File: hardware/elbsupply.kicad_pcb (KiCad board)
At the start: 2 copper layers, 105 x 64.4 mm, 80 parts, among them CON1 AVR-ISP-6, IC1 ATMEGA8-AI, P1 OUT_POS, P2 OUT_GND, P3 POWER_IN, Q1 KST2907A, SW1 SW_L, SW2 SW_R, U1 LM393, U2 TPS54331DDA, U3 LT1490, U4 LM358, U5 TS78L05CS, U6 LT3083

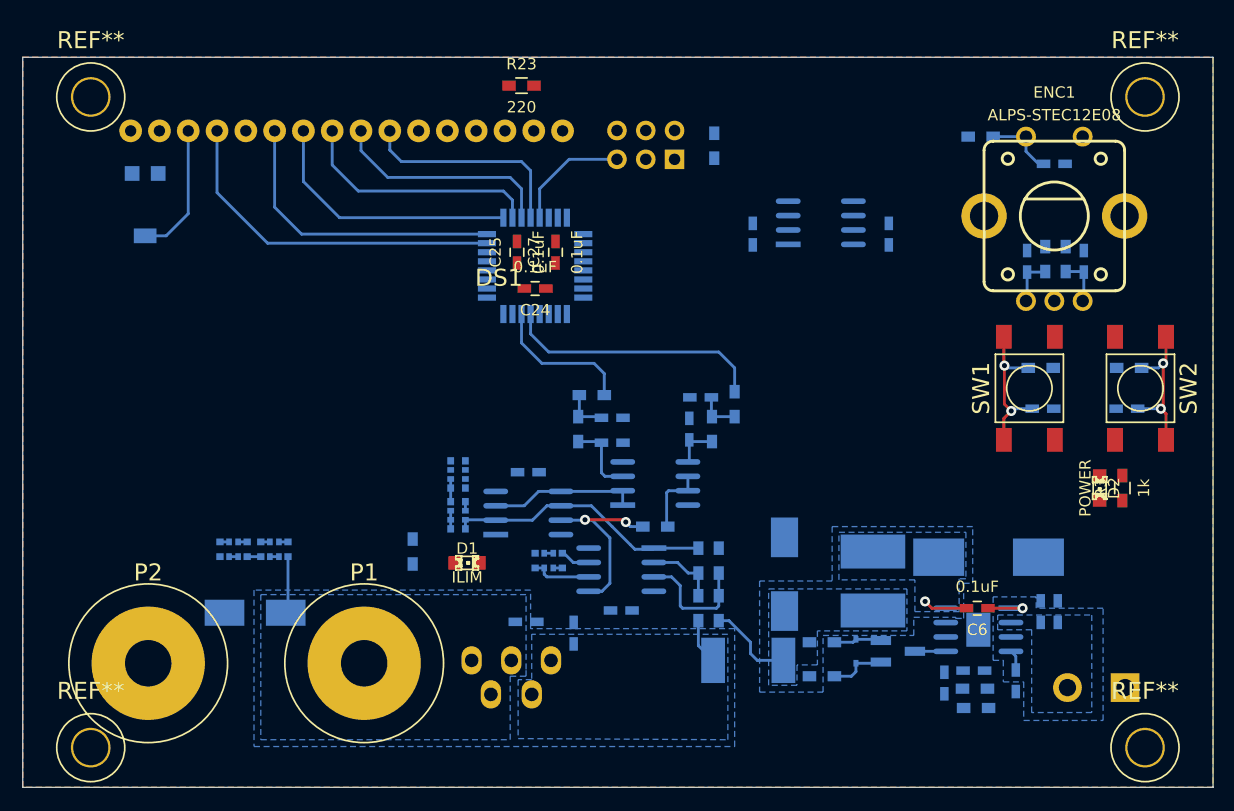
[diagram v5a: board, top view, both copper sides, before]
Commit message: LT3083 output capacitors exchanged for electrolytics
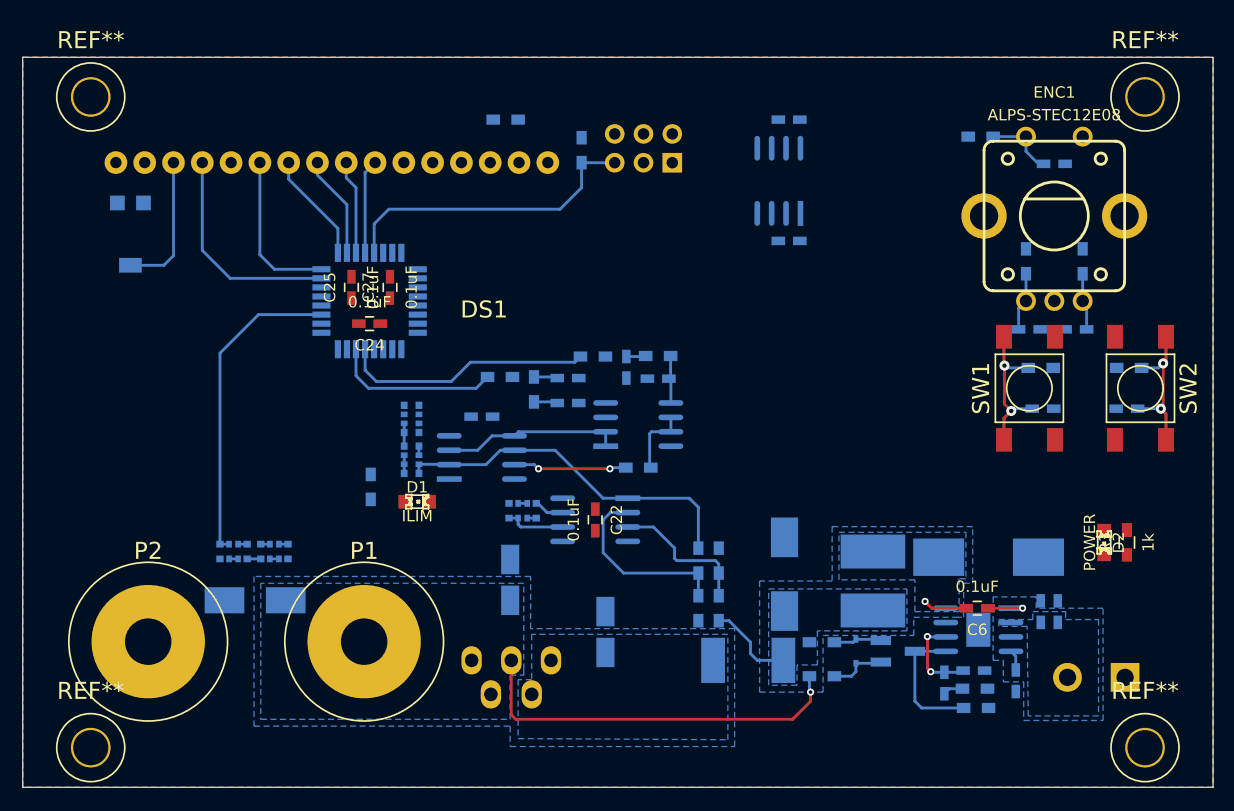
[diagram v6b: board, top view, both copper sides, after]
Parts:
- C20, C26: footprint Capacitors_SMD:C_0603_HandSoldering -> Capacitors_SMD:c_elec_4x4.5
- C22: moved to F.Cu
- R23: moved to B.Cu
- moved C24 14.9 mm to (71.6, 54.5)
- moved IC1 14.9 mm to (71.6, 52.5)
- moved C25 14.9 mm to (70.0, 51.3)
- moved C27 14.9 mm to (73.4, 51.3)
- moved C18 13.4 mm to (108.6, 36.5), turned to 180 degrees
- moved R21 13.2 mm to (91.3, 57.4), turned to 180 degrees
- moved R22 11.7 mm to (90.3, 39.2)
- moved C22 8.32 mm to (91.5, 71.8), turned to 270 degrees
- moved R7 8.26 mm to (83.1, 59.2), turned to 180 degrees
- moved R20 8.01 mm to (97.0, 57.4), turned to 180 degrees
- moved C23 7.07 mm to (94.2, 58.4), turned to 270 degrees
- moved D1 6.97 mm to (75.8, 70.2)
- moved R2 6.80 mm to (71.7, 68.9)
- moved RP3 6.39 mm to (75.3, 66.5)
- moved RP1 6.39 mm to (75.3, 62.9)
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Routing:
- net /LIN_OUT: track 5.03 -> 34.3 mm, vias 0 -> 1
- net /V_ADC: track 0.80 -> 28.0 mm
- net /~RST~: track 10.4 -> 27.3 mm
- net /LCD_D0: track 23.4 -> 9.76 mm
- net /LCD_D1: track 21.7 -> 9.04 mm
- net /LCD_E: track 26.4 -> 14.1 mm
- net /LCD_RS: track 31.1 -> 19.3 mm
- net /LCD_D2: track 19.9 -> 8.32 mm
- net /LCD_D3: track 19.0 -> 8.32 mm
- net Net-(R17-Pad2): track 6.31 -> 16.5 mm
- net Net-(Q1-Pad3): track 2.73 -> 11.7 mm
- net /I_Meas: track 23.5 -> 31.7 mm
- net Net-(C4-Pad2): track 0.00 -> 7.80 mm, vias 0 -> 2
- net /V_control: track 16.6 -> 10.0 mm
- net Net-(C14-Pad1): track 6.75 -> 2.09 mm
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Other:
- net class Default: via_dia 0.889 -> 0.635; via_drill 0.635 -> 0.381
- rule via_min_drill: 0.508 -> 0.3302
- rule via_min_size: 0.889 -> 0.508

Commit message: rev. A routing finished
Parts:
- D2: value POWER -> (none)
- ENC1: value ALPS-STEC12E08 -> (none)
- R2, R22: moved to F.Cu
- R3: moved to B.Cu
- moved D2 33.8 mm to (141.5, 40.4), turned to 90 degrees
- moved R3 29.5 mm to (134.5, 44.6)
- moved R22 18.3 mm to (73.1, 45.5), turned to 0 degrees
- moved R2 15.8 mm to (61.6, 56.8)
- moved D1 15.6 mm to (61.4, 76.2)
- moved R4 7.94 mm to (126.7, 51.6), turned to 270 degrees
- moved R6 7.72 mm to (129.5, 44.6), turned to 90 degrees
- moved R5 7.12 mm to (137.3, 51.4), turned to 270 degrees
- moved C9 6.88 mm to (133.9, 56.8)
- moved C7 5.34 mm to (129.8, 56.8)
- moved C24 3.21 mm to (71.8, 51.3), turned to 270 degrees
- moved R23 2.20 mm to (85.8, 36.4), turned to 180 degrees
- moved C6 0.40 mm to (125.2, 79.2)
- moved C25 0.20 mm to (70.2, 51.3)
- moved C17 0.10 mm to (81.5, 62.6)
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- renumbered REF** to M3
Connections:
- IC1 pad 1: /ENC_A -> /ENC_B
- IC1 pad 2: /ENC_B -> /ENC_A
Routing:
- net +24V: track 0.00 -> 199.3 mm, vias 0 -> 4
- net +5V: track 0.00 -> 142.1 mm, vias 0 -> 2
- net /SW_R: track 13.6 -> 75.7 mm
- net /ENC_SW: track 6.21 -> 67.0 mm, vias 0 -> 1
- net /ENC_B: track 5.26 -> 66.0 mm, vias 0 -> 1
- net /ENC_A: track 5.31 -> 60.4 mm, vias 0 -> 1
- net /SW_L: track 13.8 -> 63.1 mm
- net GND: track 0.00 -> 44.8 mm, vias 0 -> 26
- net /MOSI: track 0.00 -> 44.2 mm, vias 0 -> 1
- net /MISO: track 0.00 -> 41.7 mm, vias 0 -> 1
- net /SCK: track 0.00 -> 40.3 mm, vias 0 -> 1
- net Net-(D1-Pad2): track 0.00 -> 22.0 mm, vias 0 -> 1
- net /I_ADC: track 1.60 -> 22.8 mm, vias 0 -> 2
- net Net-(RP2-Pad8): track 2.66 -> 22.9 mm, vias 0 -> 1
- net Net-(D1-Pad1): track 0.00 -> 18.8 mm
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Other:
- net class Power_24V added: clearance 0.254, trace_width 0.635, via_dia 0.635, via_drill 0.381
- net class Power_5V added: clearance 0.254, trace_width 0.508, via_dia 0.635, via_drill 0.381

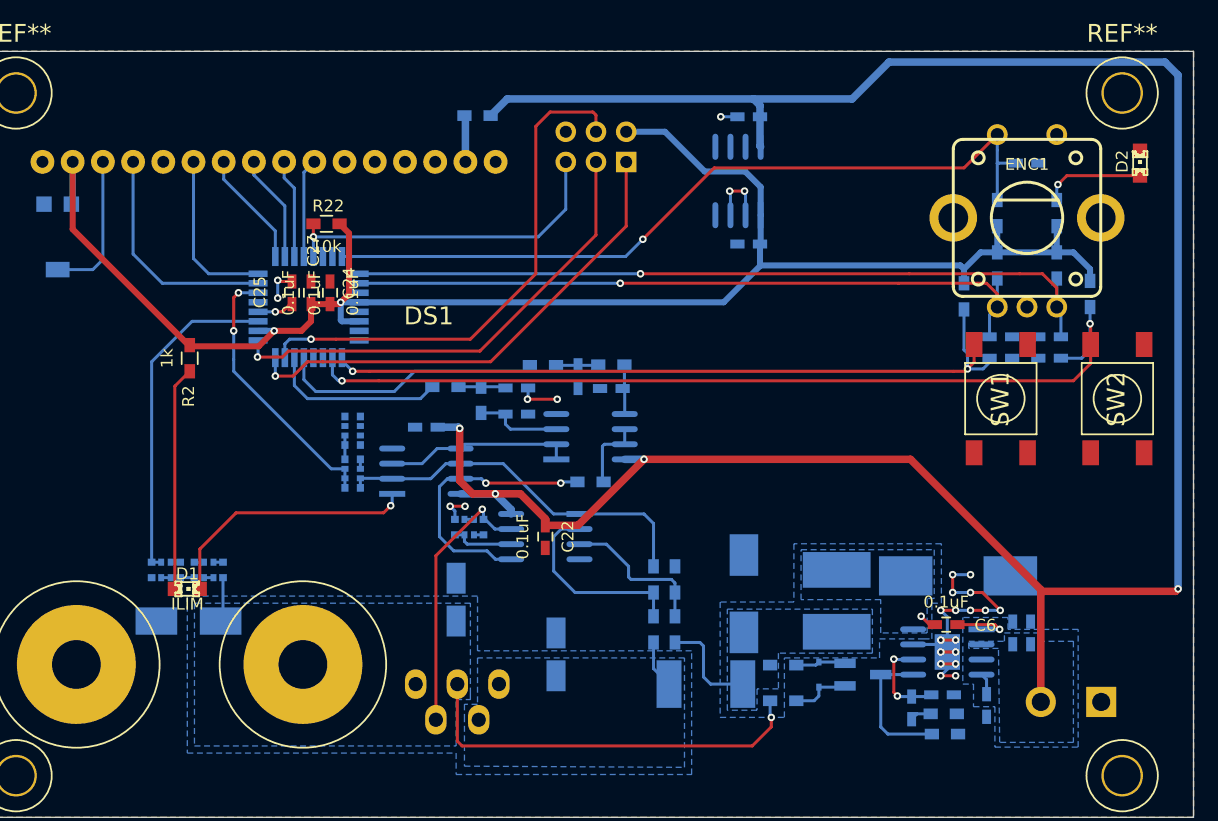
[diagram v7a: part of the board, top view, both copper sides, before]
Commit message: added two more switches for cleaner UI
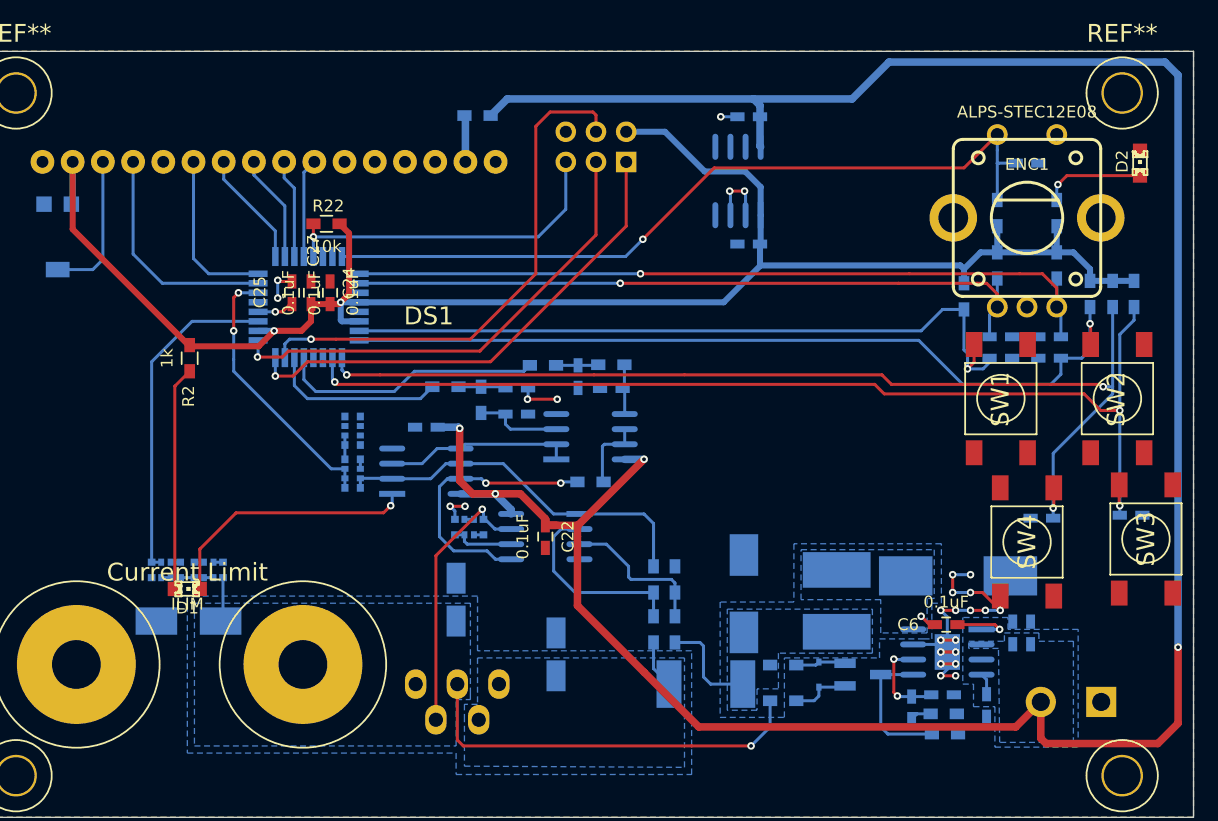
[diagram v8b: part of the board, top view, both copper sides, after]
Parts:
- added C10: 10nF, Capacitors_SMD:C_0603_HandSoldering, B.Cu at (140.8, 70.0)
- added C11: 10nF, Capacitors_SMD:C_0603_HandSoldering, B.Cu at (133.2, 70.2)
- added R24: 10k, Resistors_SMD:R_0603_HandSoldering, B.Cu at (141.0, 51.4)
- added R25: 10k, Resistors_SMD:R_0603_HandSoldering, B.Cu at (139.2, 51.4)
- added SW3: SW_OE, devthrash_KICAD:Button-SMT-standard, F.Cu at (142.0, 72.0)
- added SW4: SW_MD, devthrash_KICAD:Button-SMT-standard, F.Cu at (132.0, 72.2)
- D2: value (none) -> POWER
- ENC1: value (none) -> ALPS-STEC12E08
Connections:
- IC1 pad 10: /SW_R -> /SW_OE
- IC1 pad 7: Net-(IC1-Pad7) -> /SW_L
- IC1 pad 8: Net-(IC1-Pad8) -> /SW_R
- IC1 pad 9: /SW_L -> /SW_MD
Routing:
- net /SW_OE: track 0.00 -> 88.9 mm, vias 0 -> 3
- net /SW_MD: track 0.00 -> 88.2 mm, vias 0 -> 3
- net +24V: track 199.3 -> 218.9 mm
- net /SW_R: track 75.7 -> 70.3 mm, vias 2 -> 1
- net +5V: track 142.1 -> 145.8 mm
- net /SW_L: track 63.1 -> 61.4 mm, vias 2 -> 1
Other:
- board text added: "Current Limit"
